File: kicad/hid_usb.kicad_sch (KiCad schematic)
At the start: 8 parts, among them U2 CH9329, U3 USB_C_C393939

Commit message: idk
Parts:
- removed R3: 0R_0603, PCM_4ms_Resistor:R_0402, symbol PCM_4ms_Resistor:0R_0603
- added R3: 1R, Resistor_THT:R_Axial_DIN0207_L6.3mm_D2.5mm_P10.16mm_Horizontal, symbol PCM_SL_Resistors:5.6k
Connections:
- net Vcc: now also R3.2
- net at C2.2, U2.15 (VCC): now also R3.1
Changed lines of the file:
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@@
 	(wire
 		(pts
-			(xy 137.16 59.69) (xy 140.97 59.69)
+			(xy 135.89 59.69) (xy 140.97 59.69)
 		)
 		(stroke
@@
 	(wire
 		(pts
-			(xy 121.92 59.69) (xy 129.54 59.69)
+			(xy 121.92 59.69) (xy 128.27 59.69)
 		)
 		(stroke
@@
 	)
 	(symbol
-		(lib_id "PCM_4ms_Resistor:0R_0603")
-		(at 133.35 59.69 90)
+		(lib_id "PCM_SL_Resistors:5.6k")
+		(at 132.08 59.69 0)
 		(unit 1)
 		(exclude_from_sim no)
@@
 		(on_board yes)
 		(dnp no)
-		(fields_autoplaced yes)
 		(property "Reference" "R3"
-			(at 133.35 53.34 90)
-			(effects
-				(font
-					(size 1.27 1.27)
-				)
-			)
-		)
-		(property "Value" "0R_0603"
-			(at 133.35 62.23 90)
-			(effects
-				(font
-					(size 1.27 1.27)
-				)
-				(hide yes)
-			)
-		)
-		(property "Footprint" "PCM_4ms_Resistor:R_0402"
-			(at 146.05 62.23 0)
-			(effects
-				(font
-					(size 1.27 1.27)
-				)
-				(justify left)
+			(at 132.08 57.912 0)
+			(effects
+				(font
+					(size 1.27 1.27)
+				)
+			)
+		)
+		(property "Value" "1R"
+			(at 132.08 59.944 0)
+			(effects
+				(font
+					(size 1.27 1.27)
+				)
+			)
+		)
+		(property "Footprint" "Resistor_THT:R_Axial_DIN0207_L6.3mm_D2.5mm_P10.16mm_Horizontal"
+			(at 132.969 64.008 0)
+			(effects
+				(font
+					(size 1.27 1.27)
+				)
 				(hide yes)
 			)
 		)
 		(property "Datasheet" ""
-			(at 133.35 59.69 0)
-			(effects
-				(font
-					(size 1.27 1.27)
-				)
-				(hide yes)
-			)
-		)
-		(property "Description" "0R, 1%, 1/10W, 0603"
-			(at 133.35 59.69 0)
-			(effects
-				(font
-					(size 1.27 1.27)
-				)
-				(hide yes)
-			)
-		)
-		(property "Specifications" "0R, 1%, 1/10W, 0603"
-			(at 141.224 62.23 0)
-			(effects
-				(font
-					(size 1.27 1.27)
-				)
-				(justify left)
-				(hide yes)
-			)
-		)
-		(property "Manufacturer" "Yageo"
-			(at 142.748 62.23 0)
-			(effects
-				(font
-					(size 1.27 1.27)
-				)
-				(justify left)
-				(hide yes)
-			)
-		)
-		(property "Part Number" "RC0603FR-100RL"
-			(at 144.272 62.23 0)
-			(effects
-				(font
-					(size 1.27 1.27)
-				)
-				(justify left)
-				(hide yes)
-			)
-		)
-		(property "Display" "1R"
-			(at 133.35 55.88 90)
-			(effects
-				(font
-					(size 1.27 1.27)
-				)
-			)
-		)
-		(property "JLCPCB ID" "C21189"
-			(at 133.35 59.69 0)
-			(effects
-				(font
+			(at 132.588 59.69 0)
+			(effects
+				(font
+					(size 1.27 1.27)
+				)
+				(hide yes)
+			)
+		)
+		(property "Description" "5.6kΩ, 1/4W Resistor"
+			(at 132.08 59.69 0)
+			(effects
+				(font

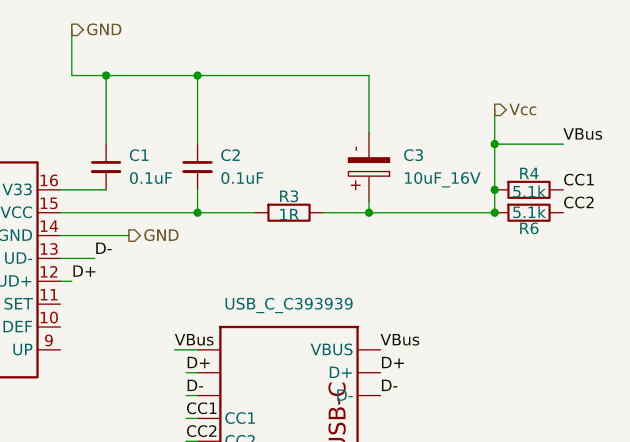
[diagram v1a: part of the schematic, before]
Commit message: switches change
switches no longer use heirarchical schematic
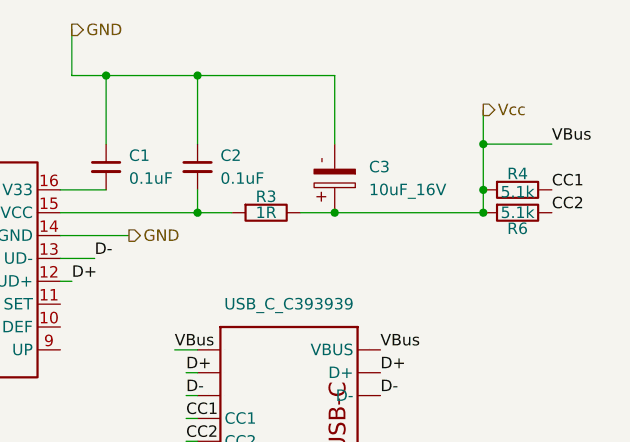
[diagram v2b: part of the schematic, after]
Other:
- moved on the sheet: C3, R3, R4, R6
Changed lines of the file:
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@@
-	)
-	(junction
-		(at 140.97 59.69)
-		(diameter 0)
-		(color 0 0 0 0)
 	)
 	(junction
@@
 	)
 	(junction
-		(at 154.94 57.15)
+		(at 153.67 57.15)
 		(diameter 0)
 		(color 0 0 0 0)
@@
 	)
 	(junction
-		(at 154.94 52.07)
+		(at 137.16 59.69)
 		(diameter 0)
 		(color 0 0 0 0)
 	)
 	(junction
-		(at 154.94 59.69)
+		(at 153.67 52.07)
 		(diameter 0)
 		(color 0 0 0 0)
 	)
+	(junction
+		(at 153.67 59.69)
+		(diameter 0)
+		(color 0 0 0 0)
+	)
 	(wire
 		(pts
@@
 	(wire
 		(pts
-			(xy 154.94 48.26) (xy 154.94 52.07)
+			(xy 153.67 48.26) (xy 153.67 52.07)
+		)
+		(stroke
+			(width 0)
+			(type default)
+		)
+	)
+	(wire
+		(pts
+			(xy 137.16 59.69) (xy 153.67 59.69)
 		)
 		(stroke
@@
 	(wire
 		(pts
-			(xy 135.89 59.69) (xy 140.97 59.69)
-		)
-		(stroke
-			(width 0)
-			(type default)
-		)
-	)
-	(wire
-		(pts
-			(xy 154.94 57.15) (xy 154.94 59.69)
+			(xy 133.35 59.69) (xy 137.16 59.69)
+		)
+		(stroke
+			(width 0)
+			(type default)
+		)
+	)
+	(wire
+		(pts
+			(xy 153.67 57.15) (xy 153.67 59.69)
 		)
 		(stroke
@@
 	(wire
 		(pts
-			(xy 140.97 59.69) (xy 154.94 59.69)
-		)
-		(stroke
-			(width 0)
-			(type default)
-		)
-	)
-	(wire
-		(pts
 			(xy 111.76 44.45) (xy 111.76 52.07)
 		)
@@
 	(wire
 		(pts
-			(xy 140.97 59.69) (xy 140.97 58.42)
-		)
-		(stroke
-			(width 0)
-			(type default)
-		)
-	)
-	(wire
-		(pts
 			(xy 74.93 71.12) (xy 74.93 72.39)
 		)
@@
 	(wire
 		(pts
-			(xy 154.94 52.07) (xy 154.94 57.15)
+			(xy 153.67 52.07) (xy 153.67 57.15)
 		)
 		(stroke
@@
 	(wire
 		(pts
-			(xy 140.97 44.45) (xy 121.92 44.45)
-		)
-		(stroke
-			(width 0)
-			(type default)
-		)
-	)
-	(wire
-		(pts
-			(xy 121.92 59.69) (xy 128.27 59.69)
+			(xy 137.16 44.45) (xy 121.92 44.45)
+		)
+		(stroke
+			(width 0)
+			(type default)
+		)
+	)
+	(wire
+		(pts
+			(xy 121.92 59.69) (xy 125.73 59.69)
 		)
 		(stroke
@@
 	(wire
 		(pts
-			(xy 140.97 50.8) (xy 140.97 44.45)
-		)
-		(stroke
-			(width 0)
-			(type default)
-		)
-	)
-	(wire
-		(pts
-			(xy 154.94 52.07) (xy 162.56 52.07)
+			(xy 137.16 52.07) (xy 137.16 44.45)
+		)
+		(stroke
+			(width 0)
+			(type default)
+		)
+	)
+	(wire
+		(pts
+			(xy 153.67 52.07) (xy 161.29 52.07)
 		)
 		(stroke
@@
 	)
 	(label "CC1"
-		(at 162.56 57.15 0)
+		(at 161.29 57.15 0)
 		(effects
 			(font
@@
 	)
 	(label "VBus"
-		(at 162.56 52.07 0)
+		(at 161.29 52.07 0)
 		(effects
 			(font
@@
 	)
 	(label "CC2"
-		(at 162.56 59.69 0)
+		(at 161.29 59.69 0)
 		(effects
 			(font
@@
 	(hierarchical_label "Vcc"
 		(shape output)
-		(at 154.94 48.26 0)
+		(at 153.67 48.26 0)
 		(effects
 			(font
@@
 	(symbol
 		(lib_id "PCM_SL_Resistors:5.6k")
-		(at 158.75 57.15 0)
+		(at 157.48 57.15 0)
 		(unit 1)
 		(exclude_from_sim no)
@@
 		(dnp no)
 		(property "Reference" "R4"
-			(at 158.75 55.372 0)
+			(at 157.48 55.372 0)
 			(effects
 				(font
@@
 		)
 		(property "Value" "5.1k"
-			(at 158.75 57.404 0)
+			(at 157.48 57.404 0)
 			(effects
 				(font
@@
 		)
 		(property "Footprint" "Resistor_THT:R_Axial_DIN0207_L6.3mm_D2.5mm_P10.16mm_Horizontal"
-			(at 159.639 61.468 0)
+			(at 158.369 61.468 0)
 			(effects
 				(font
@@
 		)
 		(property "Datasheet" ""
-			(at 159.258 57.15 0)
+			(at 157.988 57.15 0)
 			(effects
 				(font
@@
 		)
 		(property "Description" "5.6kΩ, 1/4W Resistor"
-			(at 158.75 57.15 0)
+			(at 157.48 57.15 0)
 			(effects
 				(font
@@
 	(symbol
 		(lib_id "PCM_SL_Resistors:5.6k")
-		(at 158.75 59.69 0)
+		(at 157.48 59.69 0)
 		(unit 1)
 		(exclude_from_sim no)
@@
 		(dnp no)
 		(property "Reference" "R6"
-			(at 158.75 61.468 0)
+			(at 157.48 61.468 0)
 			(effects
 				(font
@@
 		)
 		(property "Value" "5.1k"
-			(at 158.75 59.69 0)
+			(at 157.48 59.69 0)
 			(effects
 				(font
@@
 		)
 		(property "Footprint" "Resistor_THT:R_Axial_DIN0207_L6.3mm_D2.5mm_P10.16mm_Horizontal"
-			(at 159.639 64.008 0)
+			(at 158.369 64.008 0)
 			(effects
 				(font
@@
 		)
 		(property "Datasheet" ""
-			(at 159.258 59.69 0)
+			(at 157.988 59.69 0)
 			(effects
 				(font
@@
 		)
 		(property "Description" "5.6kΩ, 1/4W Resistor"
-			(at 158.75 59.69 0)
+			(at 157.48 59.69 0)
 			(effects
 				(font
@@
 	(symbol
 		(lib_id "PCM_SL_Capacitors:10uF_16V")
-		(at 140.97 54.61 90)
+		(at 137.16 55.88 90)
 		(unit 1)
 		(exclude_from_sim no)
@@
 		(fields_autoplaced yes)
 		(property "Reference" "C3"
-			(at 144.78 53.3399 90)
+			(at 140.97 54.6099 90)
 			(effects
 				(font
@@
 		)
 		(property "Value" "10uF_16V"
-			(at 144.78 55.8799 90)
+			(at 140.97 57.1499 90)
 			(effects
 				(font
@@
 		)
 		(property "Footprint" "PCM_4ms_Capacitor:CP_Tantalum_EIA-6032-28_Kemet-C"
-			(at 144.78 53.848 0)
+			(at 140.97 55.118 0)
 			(effects
 				(font
@@
 		)
 		(property "Datasheet" ""
-			(at 140.97 54.102 0)
+			(at 137.16 55.372 0)
 			(effects
 				(font
@@
 		)
 		(property "Description" "10uF, 16V Electrolytic Capacitor"
-			(at 140.97 54.61 0)
+			(at 137.16 55.88 0)
 			(effects
 				(font
@@
 	(symbol
 		(lib_id "PCM_SL_Resistors:5.6k")
-		(at 132.08 59.69 0)
+		(at 129.54 59.69 0)
 		(unit 1)
 		(exclude_from_sim no)
@@
 		(dnp no)
 		(property "Reference" "R3"
-			(at 132.08 57.912 0)
+			(at 129.54 57.912 0)
 			(effects
 				(font
@@
 		)
 		(property "Value" "1R"
-			(at 132.08 59.944 0)
+			(at 129.54 59.69 0)
 			(effects
 				(font
@@
 		)
 		(property "Footprint" "Resistor_THT:R_Axial_DIN0207_L6.3mm_D2.5mm_P10.16mm_Horizontal"
-			(at 132.969 64.008 0)
+			(at 130.429 64.008 0)
 			(effects
 				(font
@@
 		)
 		(property "Datasheet" ""
-			(at 132.588 59.69 0)
+			(at 130.048 59.69 0)
 			(effects
 				(font
@@
 		)
 		(property "Description" "5.6kΩ, 1/4W Resistor"
-			(at 132.08 59.69 0)
-			(effects
-				(font
+			(at 129.54 59.69 0)
+			(effects
+				(font
